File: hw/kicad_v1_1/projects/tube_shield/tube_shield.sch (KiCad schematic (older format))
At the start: 5 parts, among them P1 CONN_02X12_isolate_hv, P2 CONN_01X01, P3 CONN_01X01, P4 CONN_01X01, P5 CONN_01X01

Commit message: Update
Begin work on updating for rev1.1.
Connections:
- wire segments 91 -> 93
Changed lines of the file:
@@
 	1900 3000 1200 3000
 Text Label 1250 2700 0    60   ~ 0
-N0_SEL_A
+N3_SEL_A
 Text Label 1250 2800 0    60   ~ 0
-N0_SEL_B
+N3_SEL_B
 Text Label 1250 2900 0    60   ~ 0
-N0_SEL_C
+N3_SEL_C
 Text Label 1250 3000 0    60   ~ 0
-N0_SEL_D
+N3_SEL_D
 $Comp
 L +180V #PWR04
@@
 	3100 3000 2400 3000
 Text Label 2450 2700 0    60   ~ 0
-N1_SEL_A
+N2_SEL_A
 Text Label 2450 2800 0    60   ~ 0
-N1_SEL_B
+N2_SEL_B
 Text Label 2450 2900 0    60   ~ 0
-N1_SEL_C
+N2_SEL_C
 Text Label 2450 3000 0    60   ~ 0
-N1_SEL_D
+N2_SEL_D
 Wire Wire Line
 	1900 3100 1200 3100
@@
 	1900 3400 1200 3400
 Text Label 1250 3100 0    60   ~ 0
-N2_SEL_A
+N0_SEL_A
 Text Label 1250 3200 0    60   ~ 0
-N2_SEL_B
+N0_SEL_B
 Text Label 1250 3300 0    60   ~ 0
-N2_SEL_C
+N0_SEL_C
 Text Label 1250 3400 0    60   ~ 0
-N2_SEL_D
+N0_SEL_D
 Wire Wire Line
 	800  3600 800  3550
@@
 	3100 3400 2400 3400
 Text Label 2450 3100 0    60   ~ 0
-N3_SEL_A
+N1_SEL_A
 Text Label 2450 3200 0    60   ~ 0
-N3_SEL_B
+N1_SEL_B
 Text Label 2450 3300 0    60   ~ 0
-N3_SEL_C
+N1_SEL_C
 Text Label 2450 3400 0    60   ~ 0
-N3_SEL_D
+N1_SEL_D
 Wire Wire Line
-	1900 3500 1200 3500
-Text Label 1250 3500 0    60   ~ 0
+	3100 3500 2400 3500
+Text Label 2450 3500 0    60   ~ 0
 COL_SEL
 Wire Wire Line
-	2400 3500 3650 3500
-Wire Wire Line
-	3400 3500 3400 3300
+	1050 2650 1050 3500
 $Comp
 L +5V #PWR05
 U 1 1 580473A8
-P 3400 3300
-F 0 "#PWR05" H 3400 3150 50  0001 C CNN
-F 1 "+5V" H 3400 3440 50  0000 C CNN
-F 2 "" H 3400 3300 50  0000 C CNN
-F 3 "" H 3400 3300 50  0000 C CNN
-	1    3400 3300
+P 1050 2650
+F 0 "#PWR05" H 1050 2500 50  0001 C CNN
+F 1 "+5V" H 1050 2790 50  0000 C CNN
+F 2 "" H 1050 2650 50  0000 C CNN
+F 3 "" H 1050 2650 50  0000 C CNN
+	1    1050 2650
 	1    0    0    -1
 $EndComp
@@
 L PWR_FLAG #FLG06
 U 1 1 5804751F
-P 3650 3500
-F 0 "#FLG06" H 3650 3595 50  0001 C CNN
-F 1 "PWR_FLAG" H 3650 3680 50  0000 C CNN
-F 2 "" H 3650 3500 50  0000 C CNN
-F 3 "" H 3650 3500 50  0000 C CNN
-	1    3650 3500
+P 800 3150
+F 0 "#FLG06" H 800 3245 50  0001 C CNN
+F 1 "PWR_FLAG" H 800 3330 50  0000 C CNN
+F 2 "" H 800 3150 50  0000 C CNN
+F 3 "" H 800 3150 50  0000 C CNN
+	1    800  3150
 	1    0    0    -1
 $EndComp
-Connection ~ 3400 3500
 Wire Wire Line
 	6450 1150 7100 1150
@@
 Wire Wire Line
 	6450 5050 7100 5050
+Wire Wire Line
+	1050 3500 1900 3500
+Wire Wire Line
+	800  3150 800  3250
+Wire Wire Line
+	800  3250 1050 3250
+Connection ~ 1050 3250
 $EndSCHEMATC

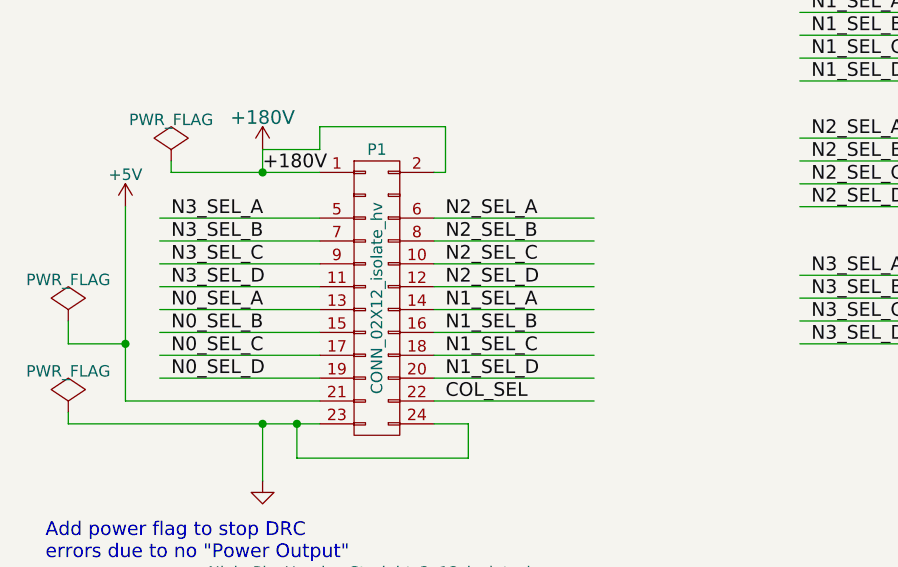
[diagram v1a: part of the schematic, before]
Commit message: Complete with errors
Check in before moving header. Currently the headers don't match up. If
I'm going to connect them with standard header I need to move it
significantly. Check in as a roll back point.
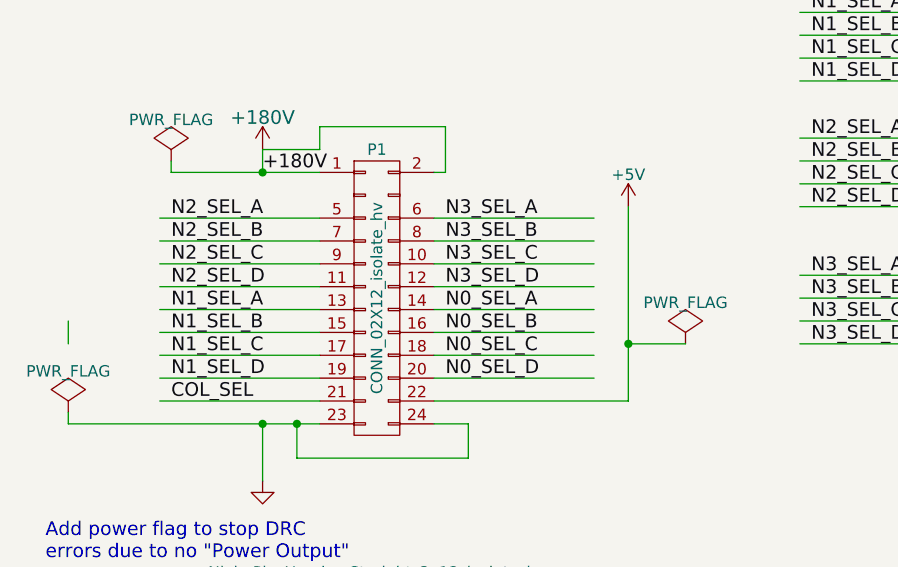
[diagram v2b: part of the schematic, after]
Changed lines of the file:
@@
 Wire Wire Line
 	1900 3000 1200 3000
-Text Label 1250 2700 0    60   ~ 0
+Text Label 2450 2700 0    60   ~ 0
 N3_SEL_A
-Text Label 1250 2800 0    60   ~ 0
+Text Label 2450 2800 0    60   ~ 0
 N3_SEL_B
-Text Label 1250 2900 0    60   ~ 0
+Text Label 2450 2900 0    60   ~ 0
 N3_SEL_C
-Text Label 1250 3000 0    60   ~ 0
+Text Label 2450 3000 0    60   ~ 0
 N3_SEL_D
 $Comp
@@
 Wire Wire Line
 	3100 3000 2400 3000
-Text Label 2450 2700 0    60   ~ 0
+Text Label 1250 2700 0    60   ~ 0
 N2_SEL_A
-Text Label 2450 2800 0    60   ~ 0
+Text Label 1250 2800 0    60   ~ 0
 N2_SEL_B
-Text Label 2450 2900 0    60   ~ 0
+Text Label 1250 2900 0    60   ~ 0
 N2_SEL_C
-Text Label 2450 3000 0    60   ~ 0
+Text Label 1250 3000 0    60   ~ 0
 N2_SEL_D
 Wire Wire Line
@@
 Wire Wire Line
 	1900 3400 1200 3400
-Text Label 1250 3100 0    60   ~ 0
+Text Label 2450 3100 0    60   ~ 0
 N0_SEL_A
-Text Label 1250 3200 0    60   ~ 0
+Text Label 2450 3200 0    60   ~ 0
 N0_SEL_B
-Text Label 1250 3300 0    60   ~ 0
+Text Label 2450 3300 0    60   ~ 0
 N0_SEL_C
-Text Label 1250 3400 0    60   ~ 0
+Text Label 2450 3400 0    60   ~ 0
 N0_SEL_D
 Wire Wire Line
@@
 Wire Wire Line
 	3100 3400 2400 3400
-Text Label 2450 3100 0    60   ~ 0
+Text Label 1250 3100 0    60   ~ 0
 N1_SEL_A
-Text Label 2450 3200 0    60   ~ 0
+Text Label 1250 3200 0    60   ~ 0
 N1_SEL_B
-Text Label 2450 3300 0    60   ~ 0
+Text Label 1250 3300 0    60   ~ 0
 N1_SEL_C
-Text Label 2450 3400 0    60   ~ 0
+Text Label 1250 3400 0    60   ~ 0
 N1_SEL_D
 Wire Wire Line
-	3100 3500 2400 3500
-Text Label 2450 3500 0    60   ~ 0
+	1900 3500 1200 3500
+Text Label 1250 3500 0    60   ~ 0
 COL_SEL
 Wire Wire Line
-	1050 2650 1050 3500
+	3250 2650 3250 3500
 $Comp
 L +5V #PWR05
 U 1 1 580473A8
-P 1050 2650
-F 0 "#PWR05" H 1050 2500 50  0001 C CNN
-F 1 "+5V" H 1050 2790 50  0000 C CNN
-F 2 "" H 1050 2650 50  0000 C CNN
-F 3 "" H 1050 2650 50  0000 C CNN
-	1    1050 2650
+P 3250 2650
+F 0 "#PWR05" H 3250 2500 50  0001 C CNN
+F 1 "+5V" H 3250 2790 50  0000 C CNN
+F 2 "" H 3250 2650 50  0000 C CNN
+F 3 "" H 3250 2650 50  0000 C CNN
+	1    3250 2650
 	1    0    0    -1
 $EndComp
@@
 L PWR_FLAG #FLG06
 U 1 1 5804751F
-P 800 3150
-F 0 "#FLG06" H 800 3245 50  0001 C CNN
-F 1 "PWR_FLAG" H 800 3330 50  0000 C CNN
-F 2 "" H 800 3150 50  0000 C CNN
-F 3 "" H 800 3150 50  0000 C CNN
-	1    800  3150
+P 3500 3250
+F 0 "#FLG06" H 3500 3345 50  0001 C CNN
+F 1 "PWR_FLAG" H 3500 3430 50  0000 C CNN
+F 2 "" H 3500 3250 50  0000 C CNN
+F 3 "" H 3500 3250 50  0000 C CNN
+	1    3500 3250
 	1    0    0    -1
 $EndComp
@@
 	6450 5050 7100 5050
 Wire Wire Line
-	1050 3500 1900 3500
+	2400 3500 3250 3500
 Wire Wire Line
 	800  3150 800  3250
 Wire Wire Line
-	800  3250 1050 3250
-Connection ~ 1050 3250
+	3250 3250 3500 3250
+Connection ~ 3250 3250
 $EndSCHEMATC

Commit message: Final Release
Update with trimming and bug fixes. This is what is being delivered as a
V1.1.0 release.
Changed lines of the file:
@@
 	6450 5050 7100 5050
 Wire Wire Line
-	2400 3500 3250 3500
+	3250 3500 2400 3500
 Wire Wire Line
 	800  3150 800  3250
